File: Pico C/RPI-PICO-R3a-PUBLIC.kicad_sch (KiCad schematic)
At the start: 38 parts, among them J3 USB_C_Receptacle_USB2.0_16P, J4 SM03B-SRSS-TB, Q1 DMG1012T-7, U2 RT6150B-33GQW, U3 W25Q16JVUXIQ, X1 ECS-120-8-33-JGN-TR

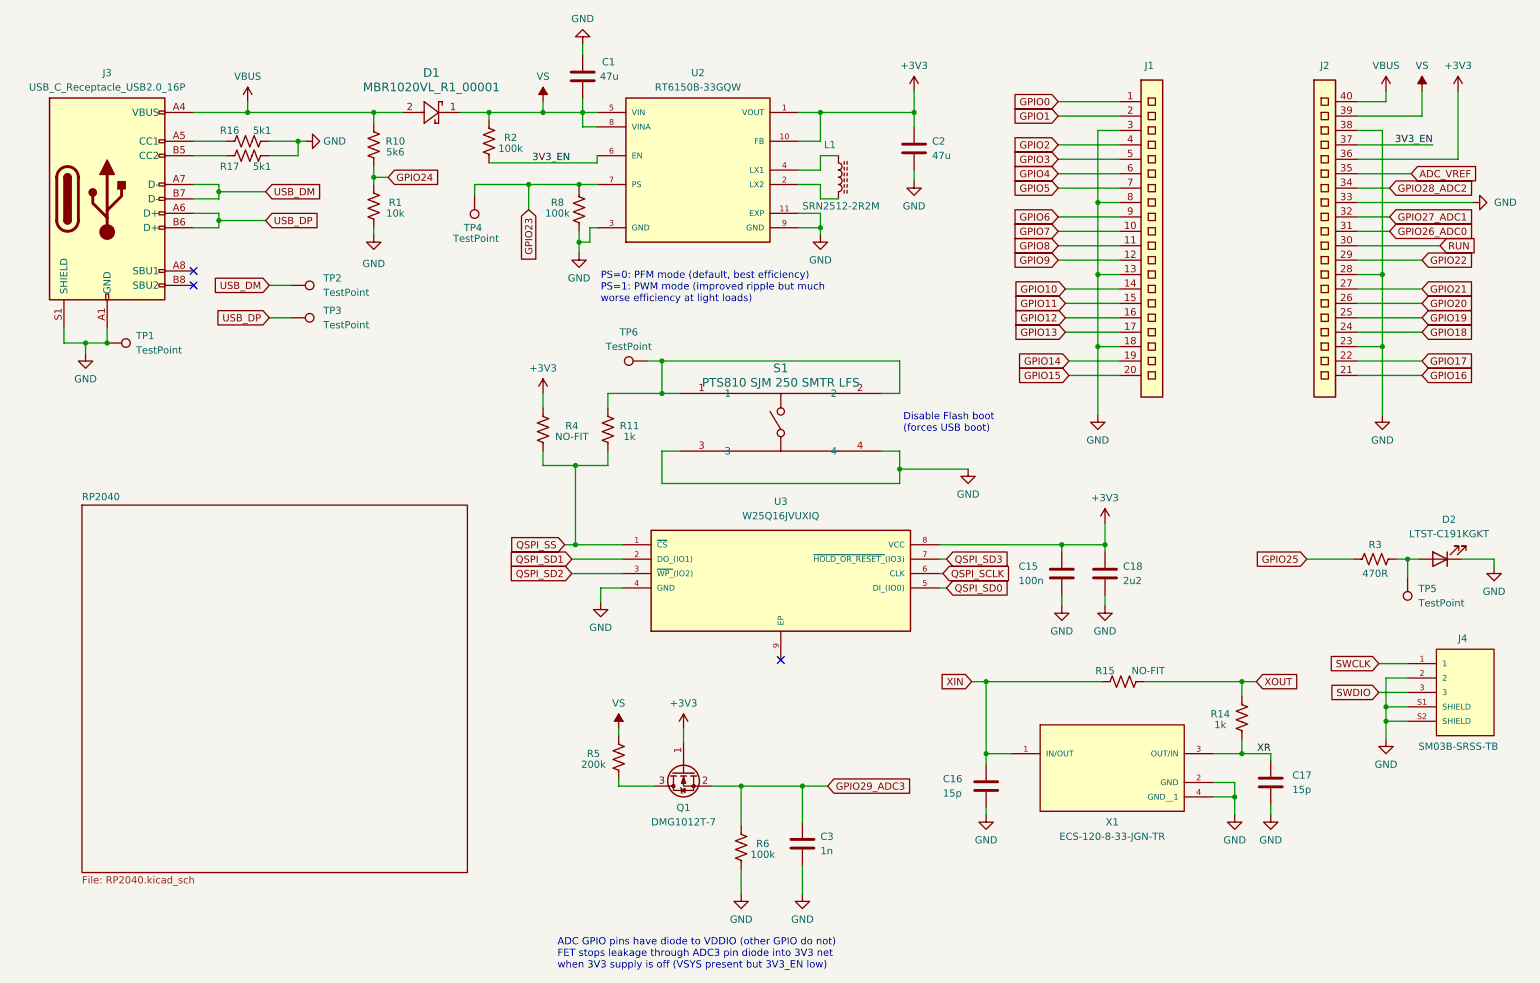
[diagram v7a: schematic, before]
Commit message: Footprint Modifications
Changed the footprints to use included KiCad models where possible, removed unnecessary STEP files.
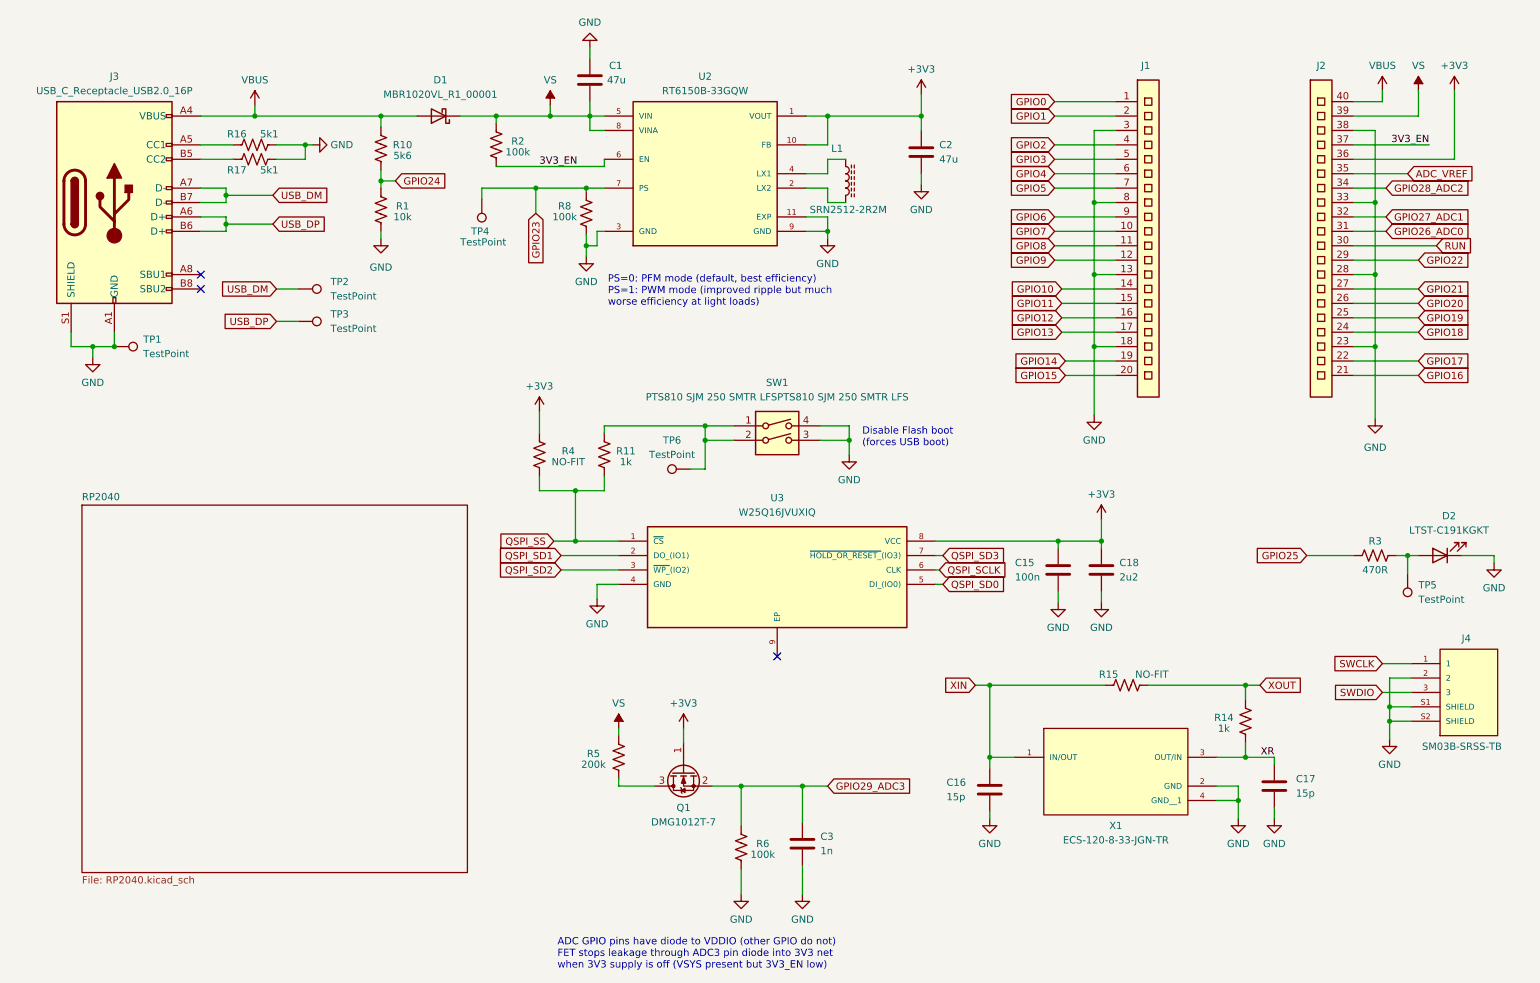
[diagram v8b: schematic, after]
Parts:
- removed D1: MBR1020VL_R1_00001, Pico_C:DIOM3616X98N, symbol Pico_C:MBR1020VL_R1_00001
- removed Q1: DMG1012T-7, Pico_C:SOT50P160X90-3N, symbol Pico_C:Q_NMOS_GSD
- removed S1: PTS810 SJM 250 SMTR LFS, Pico_C:SW_SPST_PTS810, symbol Pico_C:PTS810 SJM 250 SMTR LFS
- added D1: MBR1020VL_R1_00001, Pico_C:DIOM3616X98N, symbol Device:D_Schottky
- added Q1: DMG1012T-7, Pico_C:SOT50P160X90-3N, symbol Device:Q_NMOS_GSD
- added SW1: PTS810 SJM 250 SMTR LFSPTS810 SJM 250 SMTR LFS, Pico_C:SW_SPST_PTS810, symbol Switch:SW_DIP_x02
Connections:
- net +3V3: now also Q1.1 (G)
- net GND: now also SW1.3, SW1.4
- net GPIO29_ADC3: now also Q1.2 (S)
- net VBUS: now also D1.2 (A)
- net VS: now also D1.1 (K)
- net at R11.2, TP6.1: now also SW1.1, SW1.2
- net at R5.1: now also Q1.3 (D)
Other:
- moved on the sheet: C1, C15, C16, C17, C18, C2, D2, J1, J2, J3, J4, L1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
